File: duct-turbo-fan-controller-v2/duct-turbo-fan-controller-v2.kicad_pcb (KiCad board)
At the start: 2 copper layers, 42.7 x 53.4 mm, 26 parts, among them J1 Screw_Terminal_01x04, J2 Conn_01x04, J3 USB_OTG, J4 AudioJack4, J7 Conn_01x04, Q1 MMBT3904, Q2 BSS84, SW1 SW_Push, SW2 SW_Push, U3 ESP32-C3-WROOM-02

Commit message: Move 3.5mm jack and reduce board size. Fix GND of USB_OTG.
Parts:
- J4: moved to F.Cu
- moved J4 5.85 mm to (109.4, 86.4)
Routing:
- net +10V: track 38.5 -> 42.8 mm
- net GND: track 0.00 -> 2.15 mm
- net Net-(D1-K): track 33.6 -> 35.3 mm, vias 0 -> 1
- net +3V3: track 118.8 -> 117.1 mm
- net Tacho: track 48.4 -> 48.3 mm, vias 1 -> 2
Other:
- board size 42.7 x 53.4 mm -> 42.7 x 48.8 mm
- board text added: "DT/TB PWM Fan Controller v2.2"
- board text removed: "DT/TB PWM Fan Controller v2.1"

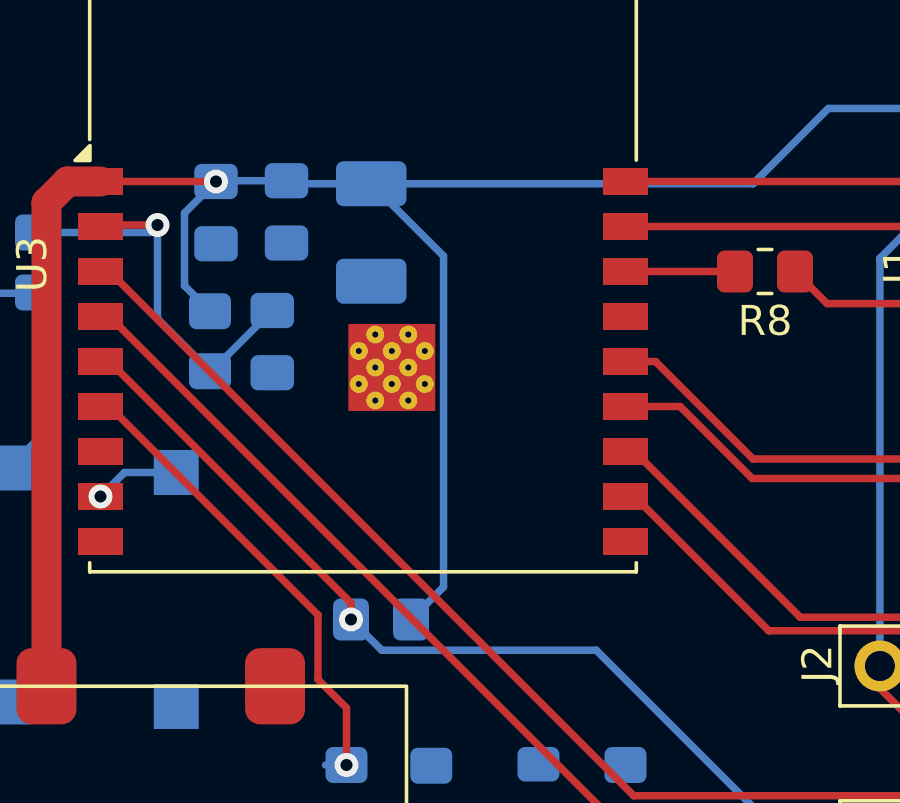
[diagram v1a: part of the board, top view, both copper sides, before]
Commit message: Move 3.3v line away from grounding thermal pad.
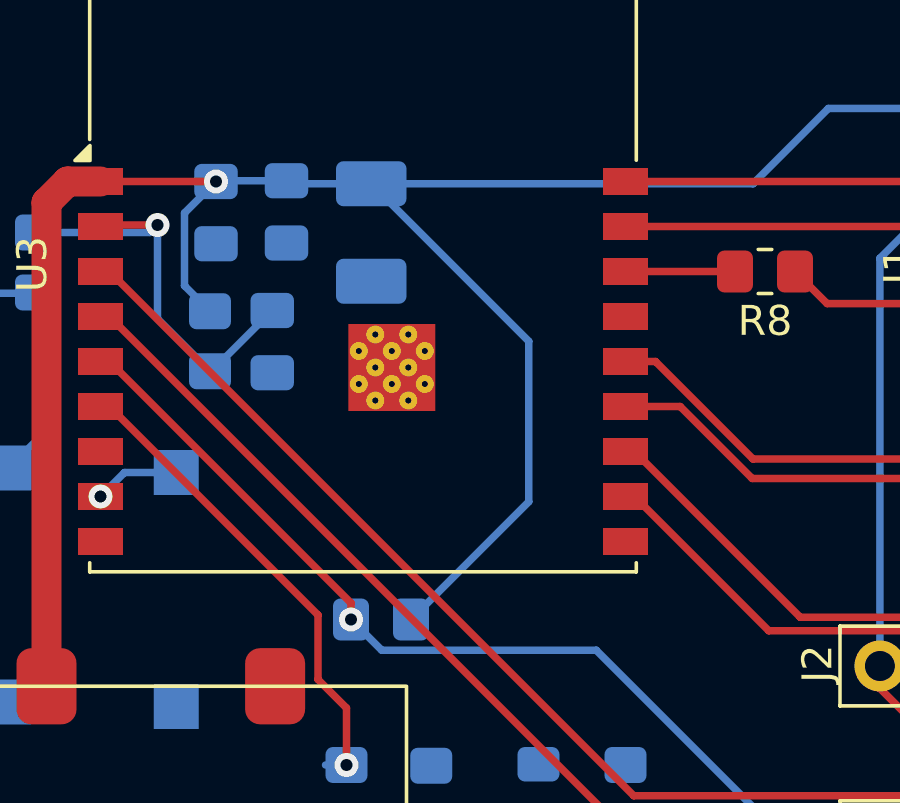
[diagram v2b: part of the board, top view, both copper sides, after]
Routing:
- net +3V3: track 117.1 -> 119.5 mm
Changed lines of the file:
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@@
 	)
 	(segment
-		(start 90.05 67.925)
-		(end 91.135 66.84)
+		(start 83.35 57.65)
+		(end 82.5 56.8)
 		(width 0.25)
 		(layer "B.Cu")
@@
 	)
 	(segment
-		(start 83.35 57.65)
-		(end 82.5 56.8)
+		(start 93.975 64)
+		(end 93.975 58.65)
 		(width 0.25)
 		(layer "B.Cu")
@@
 	)
 	(segment
-		(start 91.135 66.84)
-		(end 91.135 55.81)
-		(width 0.25)
-		(layer "B.Cu")
-		(net 4)
-	)
-	(segment
 		(start 86 53.4)
 		(end 85.9 53.3)
@@
 	)
 	(segment
-		(start 91.135 55.81)
-		(end 88.725 53.4)
+		(start 82.5 56.8)
+		(end 82.5 54.375)
 		(width 0.25)
 		(layer "B.Cu")
@@
 	)
 	(segment
-		(start 82.5 56.8)
-		(end 82.5 54.375)
+		(start 90.05 67.925)
+		(end 93.975 64)
 		(width 0.25)
 		(layer "B.Cu")
@@
 		(width 0.25)
 		(layer "B.Cu")
+		(net 4)
+	)
+	(segment
+		(start 93.975 58.65)
+		(end 88.725 53.4)
+		(width 0.25)
+		(layer "B.Cu")

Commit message: Update version number.
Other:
- board text added: "DT/TB PWM Fan Controller v2.3"
- board text removed: "DT/TB PWM Fan Controller v2.2"
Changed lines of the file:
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@@
 		(layer "Edge.Cuts")
 	)
-	(gr_text "DT/TB PWM Fan Controller v2.2"
+	(gr_text "DT/TB PWM Fan Controller v2.3"
 		(at 80.3 93.1 0)
 		(layer "F.SilkS")

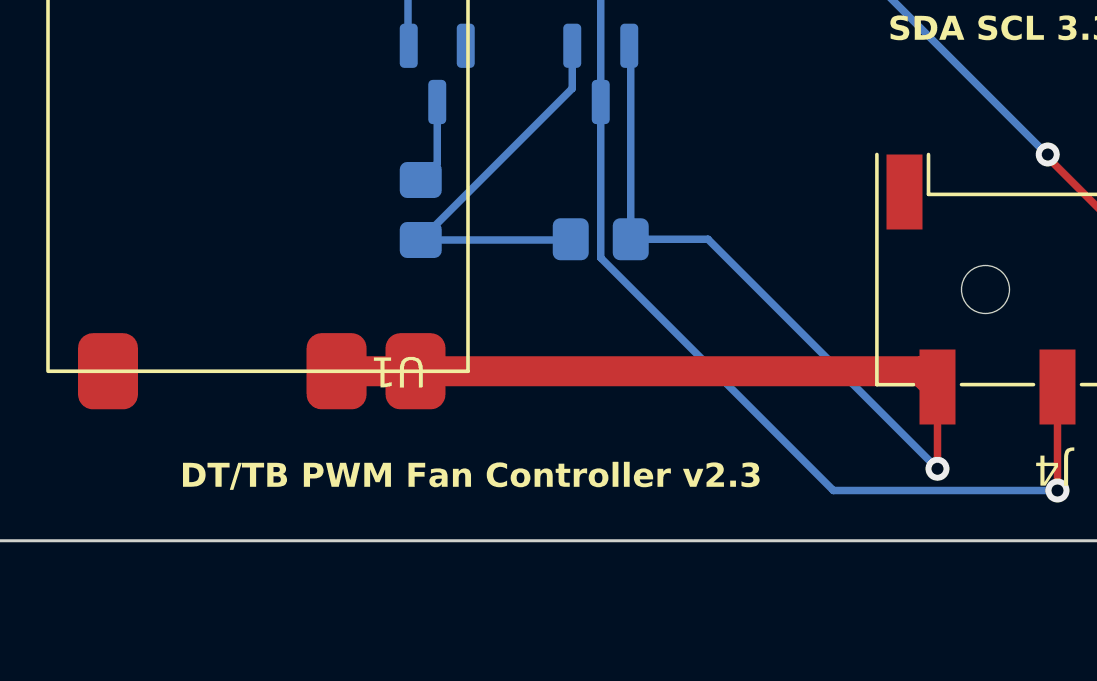
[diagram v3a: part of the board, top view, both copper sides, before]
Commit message: Add GND via on input from 3.5mm jack
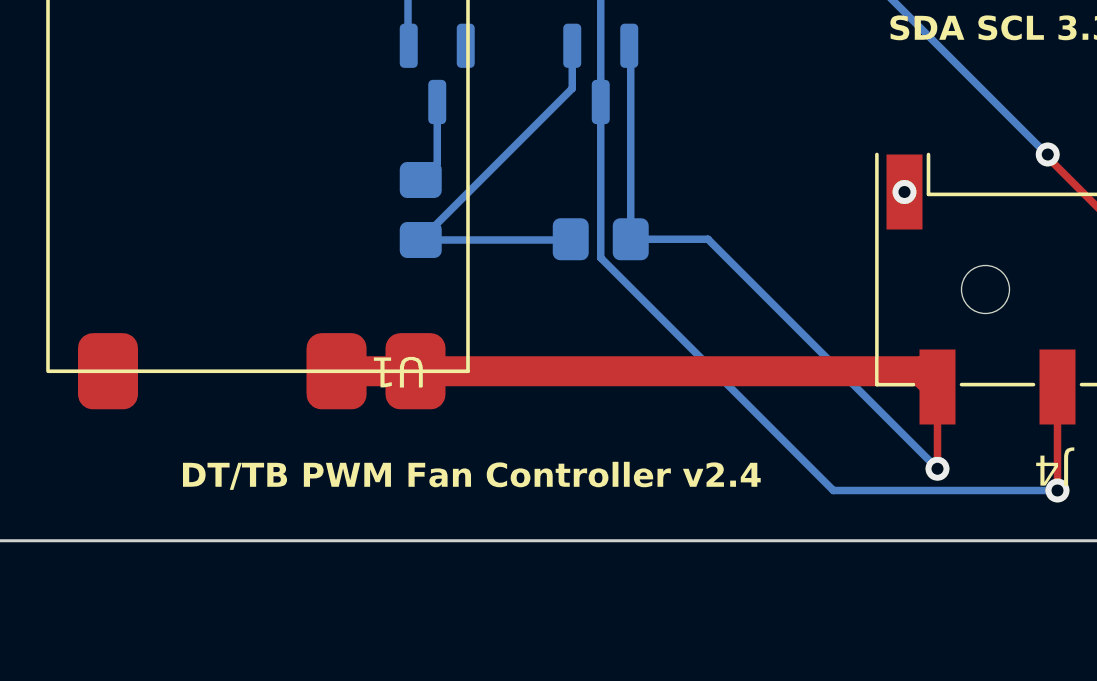
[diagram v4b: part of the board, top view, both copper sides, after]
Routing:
- net GND: vias 0 -> 1
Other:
- board text added: "DT/TB PWM Fan Controller v2.4"
- board text removed: "DT/TB PWM Fan Controller v2.3"
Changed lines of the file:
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@@
 		(layer "Edge.Cuts")
 	)
-	(gr_text "DT/TB PWM Fan Controller v2.3"
+	(gr_text "DT/TB PWM Fan Controller v2.4"
 		(at 80.3 93.1 0)
 		(layer "F.SilkS")
@@
 		(net 2)
 	)
+	(via
+		(at 104.45 83.175)
+		(size 0.8)
+		(drill 0.4)
+		(layers "F.Cu" "B.Cu")
+		(net 2)
+	)

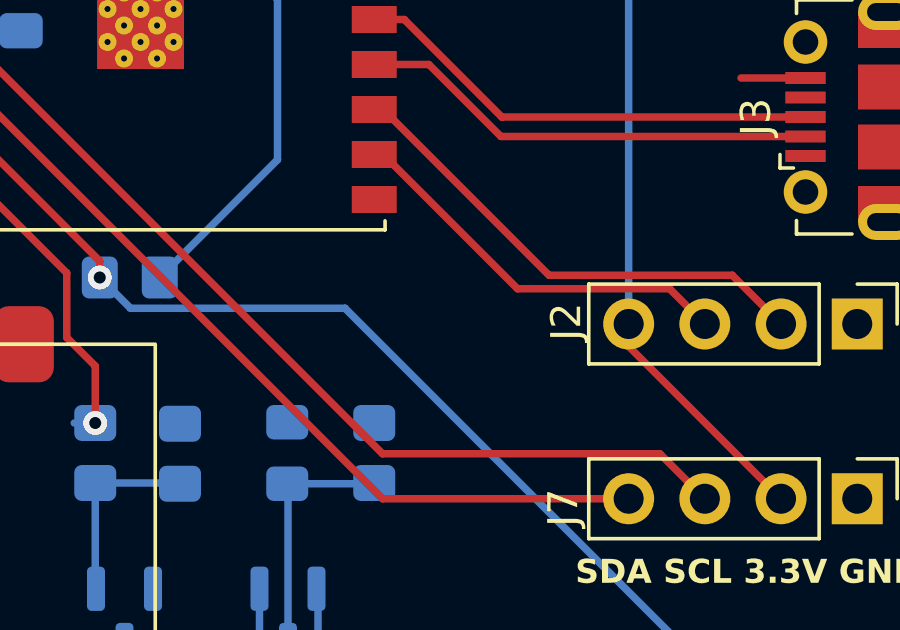
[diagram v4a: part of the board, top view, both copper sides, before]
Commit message: Add gnd via as esp32 thermal pad will not be soldered.
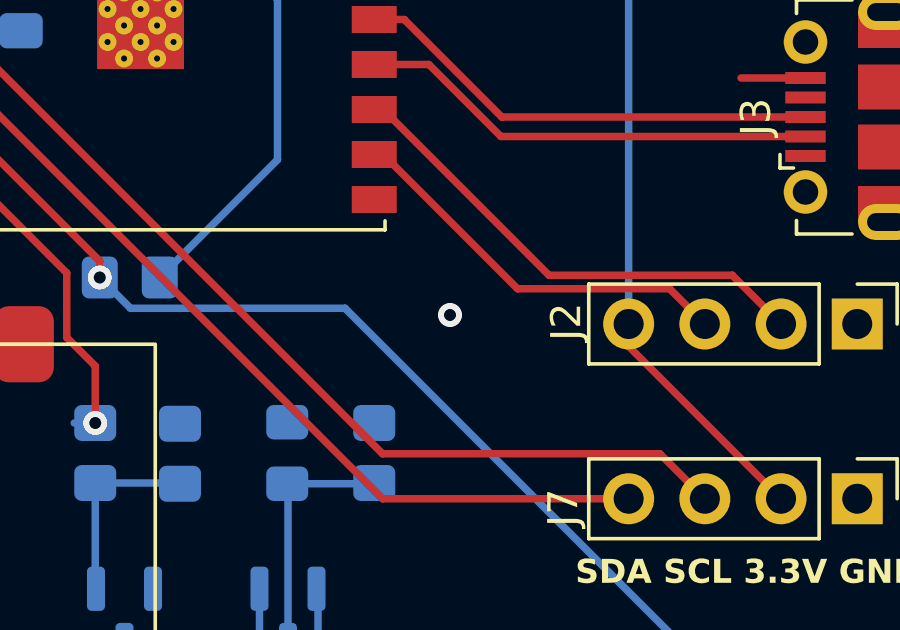
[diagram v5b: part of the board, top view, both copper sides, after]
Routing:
- net GND: vias 1 -> 2
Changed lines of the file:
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@@
+		(net 2)
+	)
+	(via
+		(at 99.725 69.175)
+		(size 0.8)
+		(drill 0.4)
+		(layers "F.Cu" "B.Cu")
+		(free yes)
 		(net 2)
 	)

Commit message: Bump board version
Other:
- board text added: "DT/TB PWM Fan Controller v2.5"
- board text removed: "DT/TB PWM Fan Controller v2.4"
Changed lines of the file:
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@@
 		(layer "Edge.Cuts")
 	)
-	(gr_text "DT/TB PWM Fan Controller v2.4"
+	(gr_text "DT/TB PWM Fan Controller v2.5"
 		(at 80.3 93.1 0)
 		(layer "F.SilkS")
